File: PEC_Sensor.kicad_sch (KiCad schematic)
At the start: 29 parts, among them IC1 TC4420, J1 Conn_01x03_Pin, J2 Conn_01x03_Pin, Q1 NMOS, U1 AD620, U2 OPA820IDBVR, U3 LM2596S-5

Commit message: revised circuits
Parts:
- removed C_In: 680 uF, symbol Device:C
- removed C_Out: 220 uF, symbol Device:C
- removed D2: 1N5822, Diode_THT:D_DO-201AD_P15.24mm_Horizontal, symbol Diode:1N5822
- removed R_Load: 10 Ω, symbol Device:R_US
- removed U3: LM2596S-5, Package_TO_SOT_SMD:TO-263-5_TabPin3, symbol Regulator_Switching:LM2596S-5
- added BT1: 12V Battery, symbol Device:Battery_Cell
- added C10: 0.1 uF, symbol Device:C_Small
- added C11: 39 pF, symbol Device:C_Small
- added C12: 4.7 nF, symbol Device:C_Small
- added C6: 10 uF, symbol Device:C_Small
- added C7, C8: 33 uF, symbol Device:C_Small
- added C9: 10 nF, symbol Device:C_Small
- added D2: B340A, symbol Device:D_Schottky
- added J3, J4, J5, J6, J7, J8: Conn_01x02_Pin, symbol Connector:Conn_01x02_Pin
- added R10: 68.1 kΩ, symbol Device:R_Small_US
- added R11: 49.9 kΩ, symbol Device:R_Small_US
- added R7: 10 kΩ, symbol Device:R_Small_US
- added R8: 1.91 kΩ, symbol Device:R_Small_US
- added R9: 332 kΩ, symbol Device:R_Small_US
- added U3: TPS54331, Package_SO:HVSSOP-10-1EP_3x3mm_P0.5mm_EP1.57x1.88mm_ThermalVias, symbol Regulator_Switching:TPS54336ADDA
- C3: value 0.1 uF -> 1.0 uF
- C4, C5: value 0.1 uF -> 10 nF
- EN1: value 11CEY25F243B -> 11CE
- L1: value 33 uH -> 6.8 uH
- U1: value AD620 -> AD8221
- U2: value OPA820IDBVR -> OPA820
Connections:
- net +12V: now also D1.1 (K), C6.1, J5.1 (Pin_1), J8.1 (Pin_1), R9.1, U3.2 (VIN); no longer Q1.1 (D), U1.7 (Vs+), U2.5 (V+)
- net +5V: now also U1.7 (Vs+), U2.5 (V+), C7.1, C8.1, R7.1
- net GND: now also Q1.3 (S), C11.2, C6.2, C7.2, C8.2, C9.2, D2.2 (A), J8.2 (Pin_2), R10.1, R11.1, R8.1, U3.4 (GND), U3.9 (ETPAD)
- net at L1.1: now also C10.2, D2.1 (K), U3.3 (PH)
- net at U1.2 (-): now also J3.1 (Pin_1); no longer L_Sense.1
- net at U1.3 (+): now also J3.2 (Pin_2); no longer L_Sense.2
- net at L_Driver.2: now also J6.2 (Pin_2); no longer D1.2 (A)
- new net: C10.1, U3.1 (BOOT)
- new net: C9.1, U3.8 (SS)
- new net: J6.1 (Pin_1), L_Driver.1
- new net: C11.1, C12.1, U3.6 (COMP)
- new net: BT1.1 (+), J7.1 (Pin_1)
- new net: BT1.2 (-), J7.2 (Pin_2)
- new net: C12.2, R11.2
- new net: R10.2, R9.2, U3.7 (EN)
- new net: J4.1 (Pin_1), L_Sense.1
- new net: J4.2 (Pin_2), L_Sense.2
- new net: D1.2 (A), J5.2 (Pin_2), Q1.1 (D)
- new net: R7.2, R8.2, U3.5 (VSENSE)
- no-connect marks 0 -> 2
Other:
- moved on the sheet: A1, C3, C4, C5, D1, EN1, IC1, J1, J2, L_Driver, L_Sense, Q1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

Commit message: revision 2 finished
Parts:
- added D4: LED, symbol Device:LED
- added R13: 150 Ω, symbol Device:R_US
- D1: value SS34 -> CDBA340L-HF
- Q1: value NMOS -> SSM3K336R
- renumbered C9 to C10, C10 to C9, L_Driver to L_Driver1, L_Sense to L_Sense1, RG to RG1
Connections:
- net +5V: now also R13.1
- net GND: now also D4.1 (K)
- new net: D4.2 (A), R13.2
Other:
- moved on the sheet: A1, C3, C4, C5, EN1, IC1, J1, J2, R3, R4, R5, R6

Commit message: fixed gitignore
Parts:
- A1: footprint Module:Arduino_Nano -> RF_Module:ESP32-C6-MINI-1
- RG1: footprint (none) -> Resistor_SMD:R_01005_0402Metric_Pad0.57x0.30mm_HandSolder
- U1: footprint (none) -> Package_SO:SOIC-8_3.9x4.9mm_P1.27mm
- renumbered D4 to D3
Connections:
- net +5V: now also U1.8 (Vs+); no longer U1.7 (Vs+)
- net GND: now also U1.6 (Ref); no longer U1.4 (Vs-)
- net at J3.1 (Pin_1): now also U1.1 (-); no longer U1.2 (-)
- net at J3.2 (Pin_2): now also U1.4 (+); no longer U1.3 (+)
- net at RG1.1: now also U1.3 (Rg); no longer U1.8 (Rg)
- net at RG1.2: now also U1.2 (Rg); no longer U1.1 (Rg)
- net at R1.2: now also U1.7; no longer U1.6
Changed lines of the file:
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@@
 		(dnp no)
 		(fields_autoplaced yes)
-		(property "Reference" "D4"
+		(property "Reference" "D3"
 			(at 136.2075 156.21 0)
 			(effects
@@
 			(project "PEC_Sensor"
 				(path "/66d8febf-d84d-4f79-8cb9-9dcbdb9b3b3f"
-					(reference "D4")
+					(reference "D3")
 					(unit 1)
 				)
@@
 			)
 		)
-		(property "Footprint" ""
+		(property "Footprint" "Resistor_SMD:R_01005_0402Metric_Pad0.57x0.30mm_HandSolder"
 			(at 161.036 54.356 90)
 			(effects
@@
 			)
 		)
-		(property "Footprint" "Module:Arduino_Nano"
+		(property "Footprint" "RF_Module:ESP32-C6-MINI-1"
 			(at 79.756 87.376 0)
 			(effects
@@
 			)
 		)
-		(property "Footprint" ""
+		(property "Footprint" "Package_SO:SOIC-8_3.9x4.9mm_P1.27mm"
 			(at 175.26 54.61 0)
 			(effects
@@
 		(pin "3"
 		)
+		(pin "4"
+		)
 		(pin "7"
 		)
-		(pin "4"
-		)
 		(pin "5"

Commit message: jan 29
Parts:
- removed A1: Arduino_Nano_ESP32, RF_Module:ESP32-C6-MINI-1, symbol MCU_Module:Arduino_Nano_ESP32
- removed BT1: 12V Battery, symbol Device:Battery_Cell
- removed C10: 10 nF, symbol Device:C_Small
- removed C11: 39 pF, symbol Device:C_Small
- removed C12: 4.7 nF, symbol Device:C_Small
- removed C7, C8: 33 uF, symbol Device:C_Small
- removed C9: 0.1 uF, symbol Device:C_Small
- removed D2: B340A, symbol Device:D_Schottky
- removed J1: Conn_01x03_Pin, Connector_JST:JST_EH_S3B-EH_1x03_P2.50mm_Horizontal, symbol Connector:Conn_01x03_Pin
- removed J4, J6, J7: Conn_01x02_Pin, symbol Connector:Conn_01x02_Pin
- removed L_Driver1: 100 uH, symbol Device:L
- removed L_Sense1: L, symbol Device:L
- removed R10: 68.1 kΩ, symbol Device:R_Small_US
- removed R11: 49.9 kΩ, symbol Device:R_Small_US
- removed R13: 150 Ω, symbol Device:R_US
- removed R7: 10 kΩ, symbol Device:R_Small_US
- removed R8: 1.91 kΩ, symbol Device:R_Small_US
- removed R9: 332 kΩ, symbol Device:R_Small_US
- removed U3: TPS54331, Package_SO:HVSSOP-10-1EP_3x3mm_P0.5mm_EP1.57x1.88mm_ThermalVias, symbol Regulator_Switching:TPS54336ADDA
- added C1: 0.1uF, symbol Device:C
- added C13: 10uF, Capacitor_SMD:C_0603_1608Metric, symbol Device:C
- added C14, C15: 0.1uF, Capacitor_SMD:C_0603_1608Metric, symbol Device:C
- added C2: 47uF, symbol Device:C
- added C3: 10uF, symbol Device:C
- added C5: 330nF, symbol Device:C_Small
- added C8, C9: 22uF, symbol Device:C
- added D2: LED, symbol Device:LED
- added J2, J3: Conn_01x15_Pin, Connector_PinHeader_2.54mm:PinHeader_1x15_P2.54mm_Vertical, symbol Connector:Conn_01x15_Pin
- added J6: Conn_01x03_Pin, symbol Connector:Conn_01x03_Pin
- added R10: R10, symbol Device:R_US
- added R5: 52.3kΩ, symbol Device:R_US
- added R6: 10kΩ, symbol Device:R_US
- added R9: R9, symbol Device:R_US
- added U1: AP62301WU, Package_TO_SOT_SMD:TSOT-23-6, symbol Regulator_Switching:AP62301WU
- C10: renamed from C3; value 1.0 uF -> 1.0uF; footprint (none) -> Capacitor_SMD:C_0603_1608Metric
- C11: renamed from C1; value 0.1 uF -> 0.1uF; footprint (none) -> Capacitor_SMD:C_0603_1608Metric
- C12: renamed from C2; value 0.1 uF -> 0.1uF; footprint (none) -> Capacitor_SMD:C_0603_1608Metric
- C4: value 10 nF -> 10nF
- C6: value 10 uF -> 100pF
- C7: renamed from C5; value 10 nF -> 10nF
- D1: footprint Diode_SMD:D_SMA -> (none)
- J1: renamed from J8; footprint (none) -> Connector_BarrelJack:BarrelJack_Horizontal
- J4: renamed from J3; value Conn_01x02_Pin -> Sensor Coil; footprint (none) -> Connector_JST:JST_EH_S2B-EH_1x02_P2.50mm_Horizontal
- J5: value Conn_01x02_Pin -> Driver Coil; footprint (none) -> Connector_JST:JST_EH_S2B-EH_1x02_P2.50mm_Horizontal
- J7: renamed from J2; footprint Connector_JST:JST_EH_S3B-EH_1x03_P2.50mm_Horizontal -> (none)
- L1: value 6.8 uH -> 3.3uH; footprint (none) -> Inductor_SMD:L_Taiyo-Yuden_NR-50xx
- R1: renamed from R3; value 10 kΩ -> 10kΩ
- R2: renamed from R5; value 10 kΩ -> 10kΩ
- R3: renamed from R6; value 10 kΩ -> 10kΩ
- R4: value 10 kΩ -> 10kΩ
- R7: renamed from R1; value 10.6 kΩ -> 10.6kΩ; footprint (none) -> Resistor_SMD:R_0603_1608Metric
- R8: renamed from R2; value 10.6 kΩ -> 10.6kΩ; footprint (none) -> Resistor_SMD:R_0603_1608Metric
- RG1: value 162 Ω -> 162Ω; footprint Resistor_SMD:R_01005_0402Metric_Pad0.57x0.30mm_HandSolder -> Resistor_SMD:R_0603_1608Metric
- U3: renamed from U2; footprint Package_TO_SOT_SMD:SOT-353_SC-70-5 -> Package_TO_SOT_SMD:SOT-23-5
- renumbered U1 to U2, IC1 to U4
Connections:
- net EnA: now also C7.1, J7.1 (Pin_1), R4.1; no longer C4.1, R1.2
- net EnB: now also C4.2, J7.3 (Pin_3), R1.2; no longer C7.1, R4.1
- net GND: now also C4.1, EN1.C, C1.2, C13.1, C14.1, C15.1, C2.2, C3.2, C8.2, C9.2, D2.1 (K), J2.10 (Pin_10), J2.14 (Pin_14), J2.2 (Pin_2), J3.14 (Pin_14), J3.7 (Pin_7), R6.2, U1.1 (GND); no longer C4.2, C6.2, J7.2 (Pin_2)
- net at J4.1 (Pin_1): now also U2.4 (+); no longer U2.1 (-)
- net at J4.2 (Pin_2): now also U2.1 (-); no longer U2.4 (+)
- net at L1.1: now also C5.2, U1.2 (SW)
- net at D3.2 (A): now also R10.2
- net at EN1.A: now also R3.1, R4.2
- net at EN1.B: now also R1.1, R2.1
- net at C11.1, R8.1: now also U3.3 (+); no longer U3.1 (+)
- net +12V renamed 12V
- net 12V: now also C3.1, R10.1, U1.3 (IN); no longer C6.1
- net +5V renamed 5V
- net 5V: now also C6.2, J7.2 (Pin_2), C1.1, C13.2, C14.2, C15.2, C2.1, C8.1, C9.1, J2.15 (Pin_15), J6.2 (Pin_2), R5.1, R9.1
- net Pulse renamed S3
- net S3: now also J2.4 (Pin_4)
- net V_sense renamed A0
- net A0: now also U3.1, J2.1 (Pin_1); no longer U3.3 (-)
- new net: D2.2 (A), R9.2
- new net: C6.1, R5.2, R6.1, U1.4 (FB)
- new net: C5.1, U1.6 (BST)
- new net 3V3: J2.11 (Pin_11), J3.15 (Pin_15), J3.6 (Pin_6)
- new net D0: J3.1 (Pin_1)
- new net D1: J3.2 (Pin_2)
- new net D2: J3.3 (Pin_3)
- new net D3: J3.4 (Pin_4)
- new net D5: J3.5 (Pin_5), J3.8 (Pin_8), J6.1 (Pin_1)
- new net D6: J3.9 (Pin_9), J6.3 (Pin_3)
- new net D7: J3.10 (Pin_10)
- new net D8: J3.11 (Pin_11)
- new net EN: J2.12 (Pin_12)
- new net RESET: J2.13 (Pin_13)
- new net RX: J3.12 (Pin_12)
- new net S0: J2.8 (Pin_8)
- new net S1: J2.6 (Pin_6)
- new net S2: J2.5 (Pin_5)
- new net SC: J2.7 (Pin_7)
- new net SK: J2.9 (Pin_9)
- new net TX: J3.13 (Pin_13)
- new net VOUT_USB: J2.3 (Pin_3)
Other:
- note added: "12V to 5V Buck Converter"
- note added: "Battery Connector"
- note added: "Driver Circuit"
- note added: "ESP32 Dev Board Breakout"
- note added: "Power Indicator LEDs"
- note added: "Sensor Circuit"
- note added: "Wheel Encoder Connector"
- moved on the sheet: C10, C11, C12, C4, C7, D1, EN1, J1, J4, J5, J7, Q1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

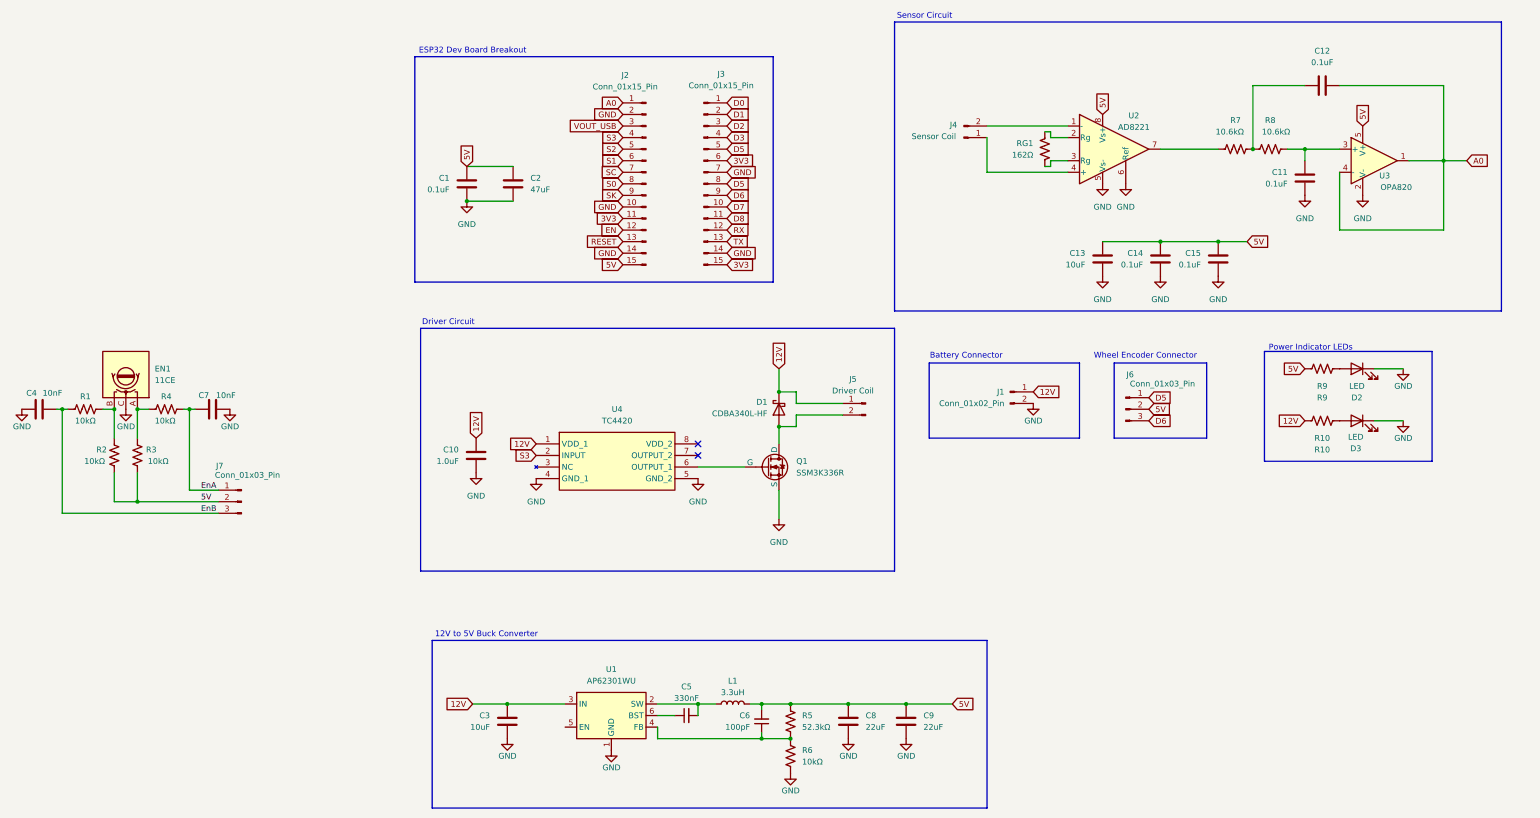
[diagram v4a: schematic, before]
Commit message: finished footprints
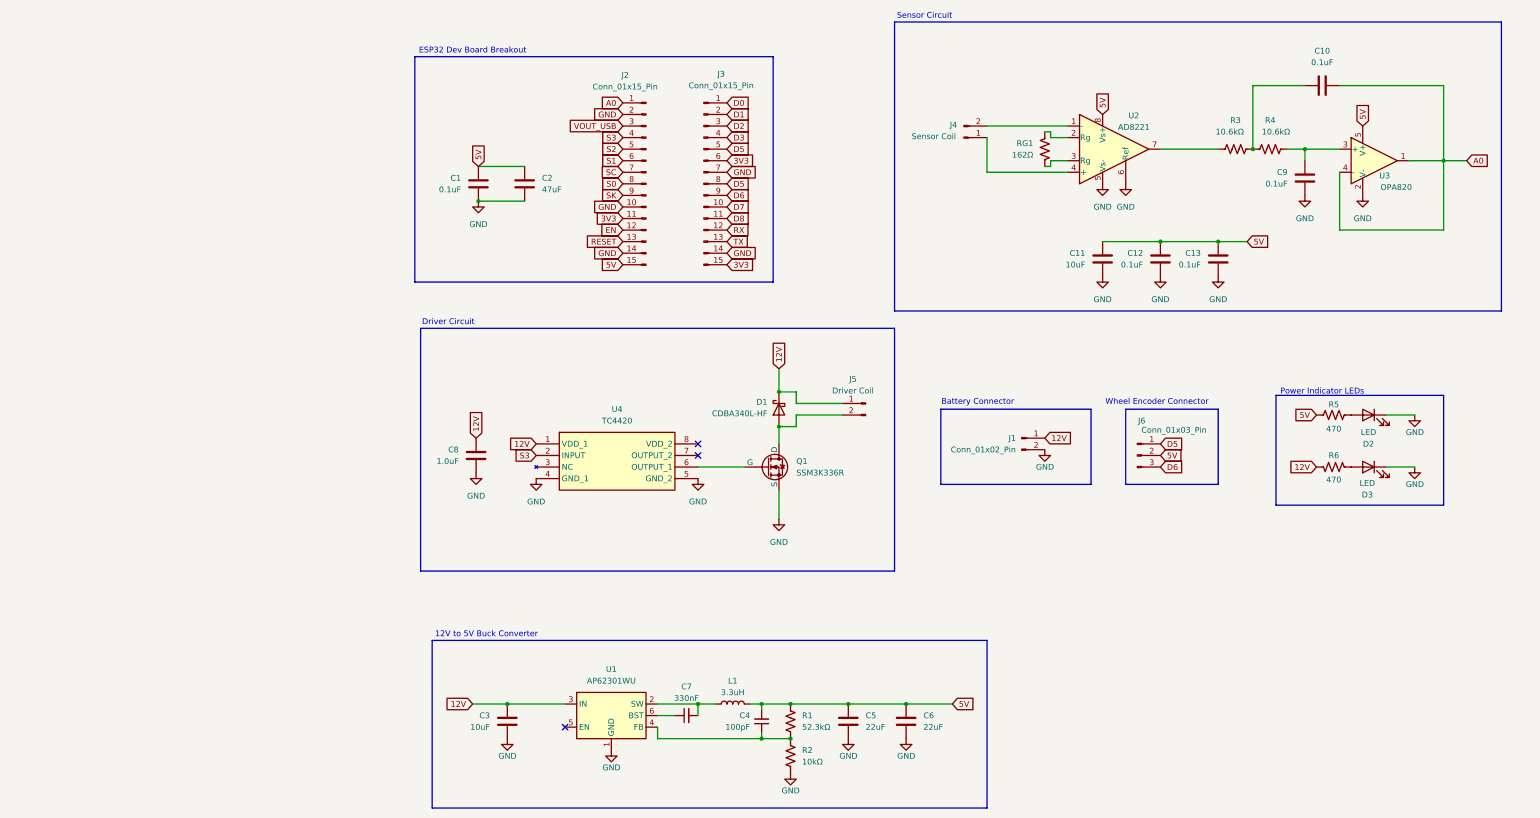
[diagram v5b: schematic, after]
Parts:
- removed C4, C7: 10nF, symbol Device:C
- removed EN1: 11CE, symbol Device:RotaryEncoder
- removed J7: Conn_01x03_Pin, symbol Connector:Conn_01x03_Pin
- removed R1, R2, R3, R4: 10kΩ, symbol Device:R_US
- C1, C2: footprint (none) -> Capacitor_SMD:C_0603_1608Metric
- C3: footprint (none) -> Capacitor_SMD:C_0805_2012Metric
- C4: renamed from C6; footprint (none) -> Capacitor_SMD:C_0603_1608Metric
- C5: renamed from C8; footprint (none) -> Capacitor_SMD:C_0805_2012Metric
- C6: renamed from C9; footprint (none) -> Capacitor_SMD:C_0805_2012Metric
- C7: renamed from C5; footprint (none) -> Capacitor_SMD:C_0603_1608Metric
- D1: footprint (none) -> Diode_SMD:D_SMA
- D2, D3: footprint (none) -> LED_SMD:LED_0603_1608Metric
- J6: footprint (none) -> Connector_JST:JST_EH_S3B-EH_1x03_P2.50mm_Horizontal
- L1: footprint Inductor_SMD:L_Taiyo-Yuden_NR-50xx -> Inductor_SMD:L_Taiyo-Yuden_NR-40xx
- Q1: footprint (none) -> Package_TO_SOT_SMD:TSOT-23
- R1: renamed from R5; footprint (none) -> Resistor_SMD:R_0603_1608Metric
- R2: renamed from R6; footprint (none) -> Resistor_SMD:R_0603_1608Metric
- R5: renamed from R9; value R9 -> 470; footprint (none) -> Resistor_SMD:R_0603_1608Metric
- R6: renamed from R10; value R10 -> 470; footprint (none) -> Resistor_SMD:R_0603_1608Metric
- renumbered C12 to C10, C13 to C11, C14 to C12, C15 to C13, C10 to C8, C11 to C9, R7 to R3, R8 to R4
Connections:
- no-connect marks 2 -> 3
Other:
- moved on the sheet: C1, C2, D2, D3, J1, J6, R5, R6

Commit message: final design done
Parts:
- removed J6: Conn_01x03_Pin, Connector_JST:JST_EH_S3B-EH_1x03_P2.50mm_Horizontal, symbol Connector:Conn_01x03_Pin
- added C14: 6.8uF, Capacitor_SMD:C_0603_1608Metric_Pad1.08x0.95mm_HandSolder, symbol Device:C
- added J6: Encoder, Connector_JST:JST_EH_S4B-EH_1x04_P2.50mm_Horizontal, symbol Connector:Conn_01x04_Pin
- added R10, R11: 100kΩ, Resistor_SMD:R_0603_1608Metric_Pad0.98x0.95mm_HandSolder, symbol Device:R_US
- added R7, R8, R9: 1kΩ, Resistor_SMD:R_0603_1608Metric_Pad0.98x0.95mm_HandSolder, symbol Device:R_US
- added RV1: 10kΩ, Potentiometer_SMD:Potentiometer_Bourns_TC33X_Vertical, symbol Device:R_Potentiometer_Trim_US
- C1, C10, C11, C12, C13, C4, C7, C8, C9: footprint Capacitor_SMD:C_0603_1608Metric -> Capacitor_SMD:C_0603_1608Metric_Pad1.08x0.95mm_HandSolder
- C2: value 47uF -> 10uF; footprint Capacitor_SMD:C_0603_1608Metric -> Capacitor_SMD:C_0603_1608Metric_Pad1.08x0.95mm_HandSolder
- C3, C5, C6: footprint Capacitor_SMD:C_0805_2012Metric -> Capacitor_SMD:C_0805_2012Metric_Pad1.18x1.45mm_HandSolder
- D1: footprint Diode_SMD:D_SMA -> Diode_SMD:D_SMA_Handsoldering
- D2: value LED -> APT2012LZGCK; footprint LED_SMD:LED_0603_1608Metric -> LED_SMD:LED_0805_2012Metric_Pad1.15x1.40mm_HandSolder
- D3: value LED -> APT2012LVBC/D; footprint LED_SMD:LED_0603_1608Metric -> LED_SMD:LED_0805_2012Metric_Pad1.15x1.40mm_HandSolder
- R1, R2, R3, R4: footprint Resistor_SMD:R_0603_1608Metric -> Resistor_SMD:R_0603_1608Metric_Pad0.98x0.95mm_HandSolder
- R5: value 470 -> 100Ω; footprint Resistor_SMD:R_0603_1608Metric -> Resistor_SMD:R_0603_1608Metric_Pad0.98x0.95mm_HandSolder
- R6: value 470 -> 470Ω; footprint Resistor_SMD:R_0603_1608Metric -> Resistor_SMD:R_0603_1608Metric_Pad0.98x0.95mm_HandSolder
- RG1: value 162Ω -> 10k; footprint Resistor_SMD:R_0603_1608Metric -> Resistor_SMD:R_0603_1608Metric_Pad0.98x0.95mm_HandSolder
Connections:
- net RX is gone; now on net D2: J3.12 (Pin_12)
- net S1 is gone; now on net D32: J2.6 (Pin_6)
- net 3V3: no longer J2.11 (Pin_11), J3.6 (Pin_6)
- net 5V: now also C14.2, J6.4 (Pin_4)
- net D2: now also J6.2 (Pin_2); no longer J3.3 (Pin_3)
- net D5: no longer J3.5 (Pin_5)
- net EN: now also J2.1 (Pin_1); no longer J2.12 (Pin_12)
- net GND: now also Q1.2 (S), C14.1, J6.1 (Pin_1), R10.2, R11.1, R7.2, RV1.3; no longer J2.10 (Pin_10), J2.2 (Pin_2), J3.7 (Pin_7), Q1.3 (S)
- net at J4.1 (Pin_1): now also R9.1; no longer U2.4 (+)
- net at J4.2 (Pin_2): now also R8.1; no longer U2.1 (-)
- net at D1.2 (A), J5.2 (Pin_2): now also Q1.3 (D); no longer Q1.1 (D)
- net at U4.6 (OUTPUT_1): now also Q1.1 (G); no longer Q1.2 (G)
- net at R3.2: now also R7.1, RV1.2; no longer U2.7
- net A0 renamed D32
- net D32: no longer J2.1 (Pin_1)
- net D0 renamed D23
- net D1 renamed D22
- net D3 renamed RX0
- net D6 renamed TX2
- net D7 renamed RX2
- net D8 renamed D4
- net D4: now also J6.3 (Pin_3)
- net RESET renamed D13
- net D13: now also U4.2 (INPUT)
- net S0 renamed D25
- net S2 renamed D35
- net S3 renamed D34
- net D34: no longer U4.2 (INPUT)
- net SC renamed D33
- net SK renamed D26
- net TX renamed D15
- net VOUT_USB renamed VN
- new net: R11.2, R9.2, U2.4 (+)
- new net: R10.1, R8.2, U2.1 (-)
- new net: RV1.1, U2.7
- new net D12: J2.12 (Pin_12)
- new net D14: J2.11 (Pin_11)
- new net D18: J3.7 (Pin_7)
- new net D19: J3.6 (Pin_6)
- new net D21: J3.5 (Pin_5)
- new net D27: J2.10 (Pin_10)
- new net TX0: J3.3 (Pin_3)
- new net VP: J2.2 (Pin_2)
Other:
- moved on the sheet: C10, C11, C12, C13, C8, C9, D1, J4, J5, Q1, R3, R4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

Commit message: updated led values
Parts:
- R5: value 100Ω -> 1kΩ
- R6: value 470Ω -> 10kΩ
- RG1: value 10k -> 10kΩ
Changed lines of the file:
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@@
 			)
 		)
-		(property "Value" "100Ω"
+		(property "Value" "1kΩ"
 			(at 220.98 109.728 90)
 			(effects
@@
 			)
 		)
-		(property "Value" "10k"
+		(property "Value" "10kΩ"
 			(at 154.94 41.9099 0)
 			(effects
@@
 			)
 		)
-		(property "Value" "470Ω"
+		(property "Value" "10kΩ"
 			(at 220.98 120.904 90)
 			(effects

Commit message: updated resistor values
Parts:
- RG1: value 10kΩ -> 470Ω
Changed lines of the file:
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@@
 	(rectangle
 		(start 20.32 90.17)
-		(end 124.46 143.51)
+		(end 130.81 143.51)
 		(stroke
 			(width 0)
@@
 			)
 		)
-		(property "Value" "10kΩ"
+		(property "Value" "470Ω"
 			(at 154.94 41.9099 0)
 			(effects
